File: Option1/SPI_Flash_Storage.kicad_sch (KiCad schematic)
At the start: 0 parts

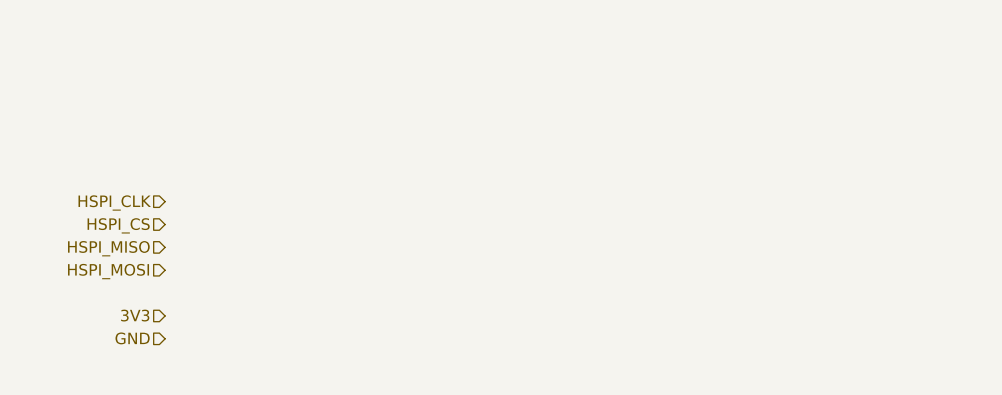
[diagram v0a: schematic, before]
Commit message: SPI Flash hinzugefügt, IN/Outputs vereinheitlicht, USB Flash Möglichkeit hinzugefügt, Display fehtl noch
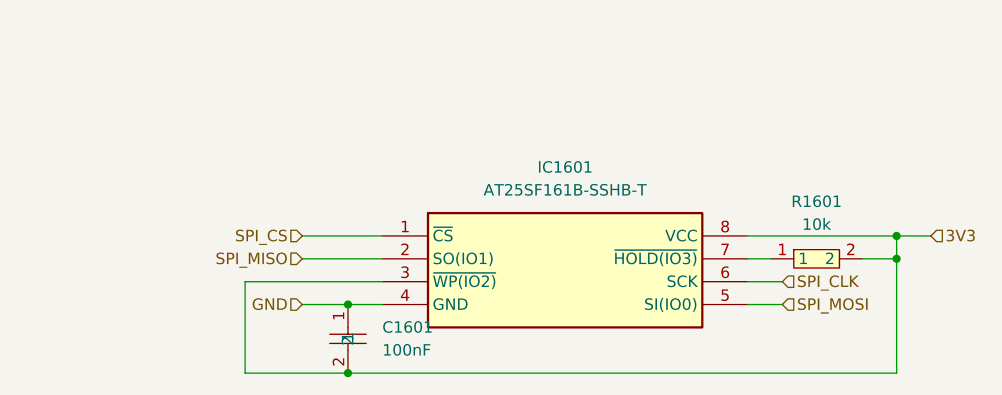
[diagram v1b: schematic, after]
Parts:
- added C1601: 100nF, easyeda2kicad:C0603, symbol easyeda2kicad:CL10B104KA8NNNC
- added IC1601: AT25SF161B-SSHB-T, SOIC127P600X175-8N, symbol SPI_Flash:AT25SF161B-SSHB-T
- added R1601: 10k, easyeda2kicad:R0603, symbol easyeda2kicad:0603WAF1002T5E
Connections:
- net 3V3: now also C1601.2, IC1601.3 (~{WP(IO2)}), IC1601.8 (VCC), R1601.2
- net GND: now also C1601.1, IC1601.4 (GND)
- new net: IC1601.7 (~{HOLD(IO3)}), R1601.1
- new net SPI_CLK: IC1601.6 (SCK)
- new net SPI_CS: IC1601.1 (~{CS})
- new net SPI_MISO: IC1601.2 (SO(IO1))
- new net SPI_MOSI: IC1601.5 (SI(IO0))

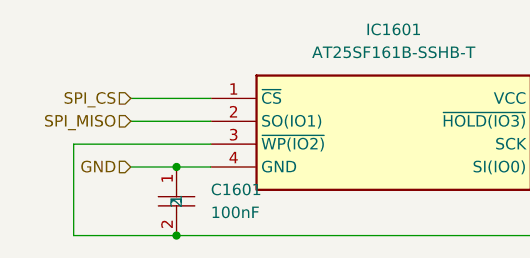
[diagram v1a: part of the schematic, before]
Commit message: USB auf 3V3 umgebaut
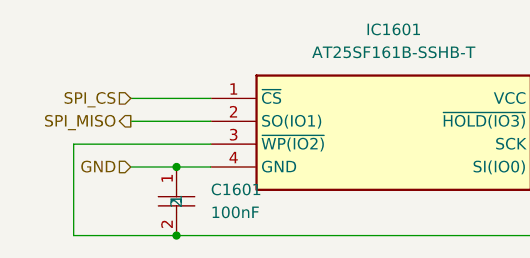
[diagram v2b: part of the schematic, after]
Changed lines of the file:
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@@
 	)
 	(hierarchical_label "SPI_MISO"
-		(shape input)
+		(shape output)
 		(at 54.61 46.99 180)
 		(effects

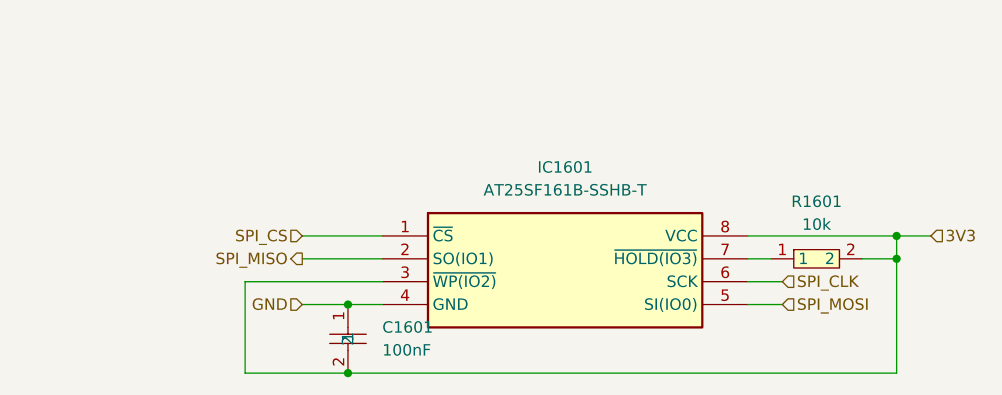
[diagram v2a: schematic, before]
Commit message: SPI Flash getauscht
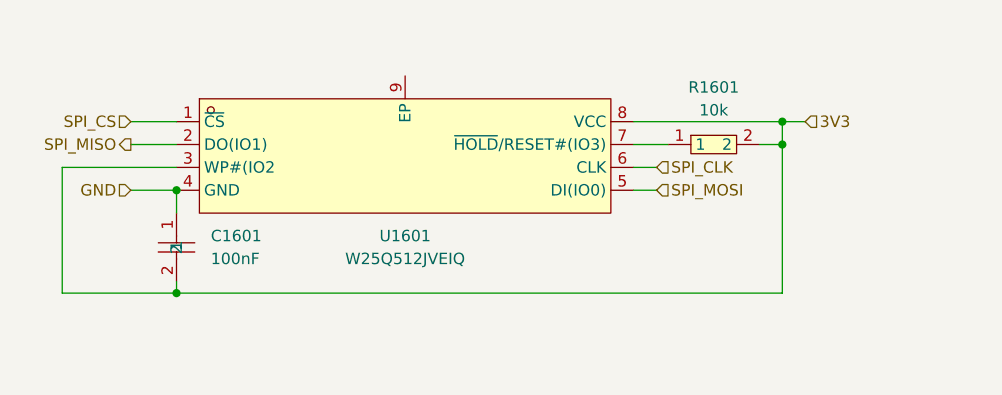
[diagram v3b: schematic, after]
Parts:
- removed IC1601: AT25SF161B-SSHB-T, SOIC127P600X175-8N, symbol SPI_Flash:AT25SF161B-SSHB-T
- added U1601: W25Q512JVEIQ, easyeda2kicad:WSON-8_L8.0-W6.0-P1.27-TL-EP, symbol EasyEda2KiCad:W25Q512JVEIQ
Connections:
- net 3V3: now also U1601.3 (WP#(IO2), U1601.8 (VCC)
- net GND: now also U1601.4 (GND)
- net SPI_CLK: now also U1601.6 (CLK)
- net SPI_CS: now also U1601.1 (~{CS})
- net SPI_MISO: now also U1601.2 (DO(IO1))
- net SPI_MOSI: now also U1601.5 (DI(IO0))
- net at R1601.1: now also U1601.7 (~{HOLD}/RESET#(IO3))
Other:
- moved on the sheet: C1601, R1601

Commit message: Kapitel über Schaltplan fortgesetzt, Fehler in Schaltplan korrigiert, DCDC getauscht, USB Schaltung angepasst, 3.3V Schaltung angepasst
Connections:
- net GND: now also U1601.9 (EP)
